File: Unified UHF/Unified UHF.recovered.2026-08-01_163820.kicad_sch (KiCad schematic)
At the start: 28 parts, among them IC6 MCP1603-330I_MC, J1 Conn_01x05, J2 Conn_01x02, J3 Conn_Coaxial, U1 AT86RF215-ZU, U3 NCS-62+, X1 TYETACSANF-26.000000

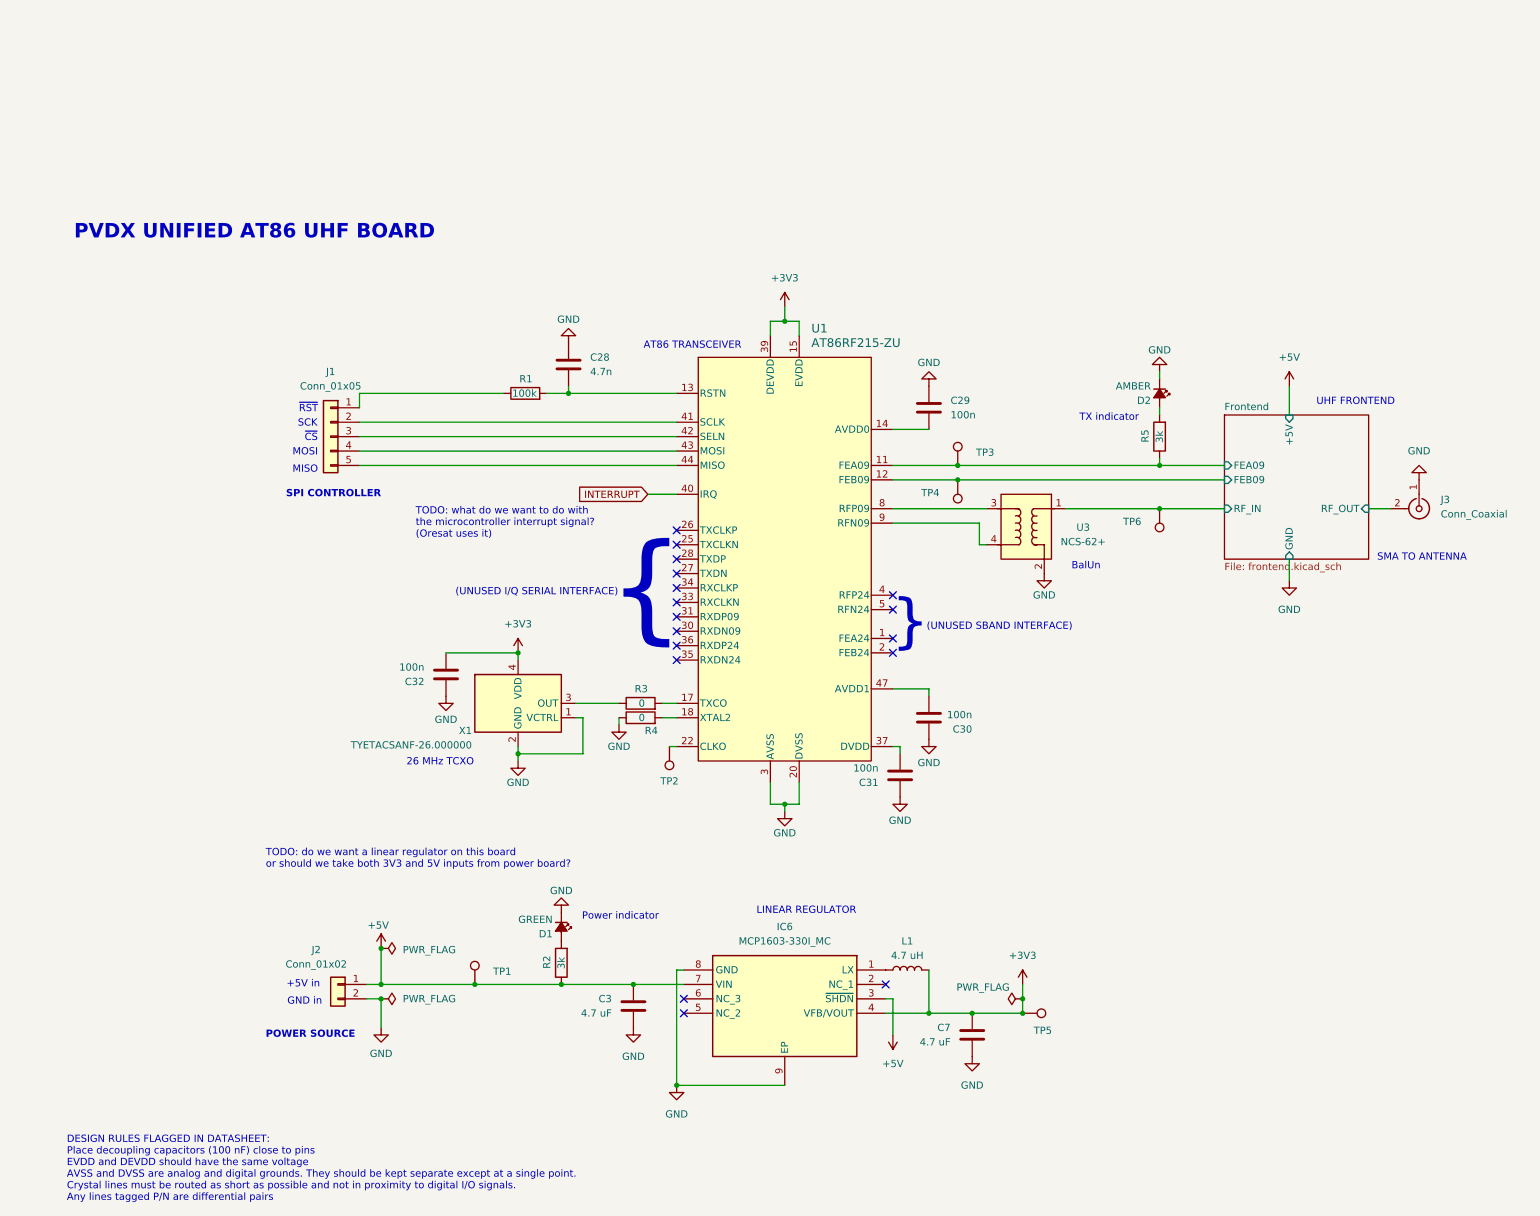
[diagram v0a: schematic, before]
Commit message: added unified radio schematic
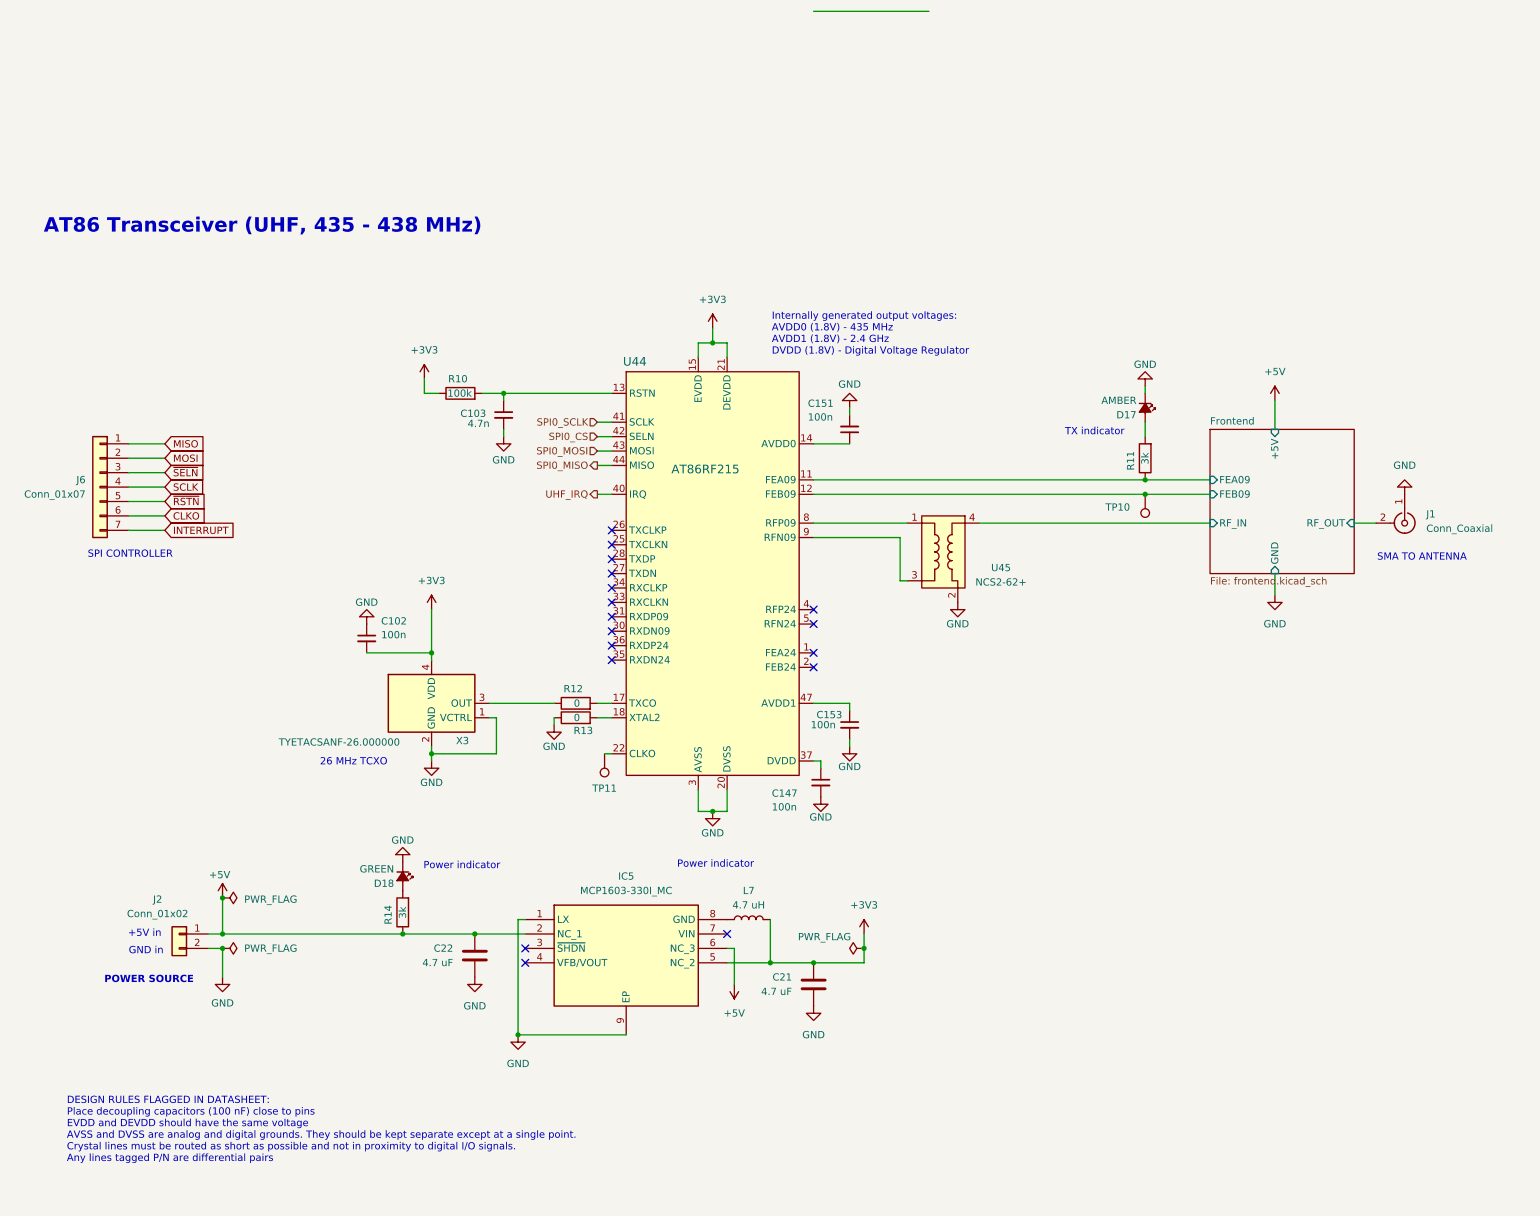
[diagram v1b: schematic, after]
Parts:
- removed C28: 4.7n, symbol Device:C
- removed C29, C30, C31, C32: 100n, symbol Device:C
- removed IC6: MCP1603-330I_MC, MCP1603:MCP1603-330, symbol MCP1603:MCP1603-330I_MC
- removed J1: Conn_01x05, symbol Connector_Generic:Conn_01x05
- removed TP1, TP3, TP5, TP6: TestPoint, TestPoint:TestPoint_THTPad_1.5x1.5mm_Drill0.7mm, symbol Connector:TestPoint
- removed U1: AT86RF215-ZU, RF Frontend Footprints:QFN-48-1EP_7x7mm_P0.5mm_EP5.6x5.6mm, symbol AT86RF215:AT86RF215-ZU
- removed U3: NCS-62+, RF Frontend Footprints:NCS262, symbol NCS2-62+:NCS2-62+_Custom
- removed X1: TYETACSANF-26.000000, RF Frontend Footprints:X_TCXO_SMD_Taitien_2.5x2.0mm, symbol TYETACSANF-26.000000:Taiten-TY-Series-TXCO
- added C102, C147, C151, C153: 100n, oresat-passives:0603-C-NOSILK, symbol Device:C_Small
- added C103: 4.7n, oresat-passives:0603-C-NOSILK, symbol Device:C_Small
- added IC5: MCP1603-330I_MC, MPC1603:MPC1603-330, symbol MCP1603:MCP1603-330I_MC
- added J6: Conn_01x07, symbol Connector_Generic:Conn_01x07
- added U44: AT86RF215, Package_DFN_QFN:QFN-48-1EP_7x7mm_P0.5mm_EP5.6x5.6mm, symbol oresat-ics:AT86RF215
- added U45: NCS2-62+, oresat-passives:2450FB15A050E_JOT, symbol oresat-passives:Balun
- added X3: TYETACSANF-26.000000, oresat-ics:X_TCXO_SMD_Taitien_2.5x2.0mm, symbol oresat-ics:Taiten-TY-Series-TXCO
- renumbered C7 to C21, C3 to C22, D2 to D17, D1 to D18, J3 to J1, L1 to L7, R1 to R10, R5 to R11, R3 to R12, R4 to R13, R2 to R14, TP4 to TP10, TP2 to TP11
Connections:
- net +3V3: now also R10.1, C102.2, IC5.5 (NC_2), U44.15 (EVDD), U44.21 (DEVDD), U44.29 (DEVDD), U44.39 (DEVDD), U44.46 (EVDD), X3.4 (VDD)
- net +5V: now also IC5.2 (NC_1), IC5.6 (NC_3)
- net Frontend/FEA09: now also U44.11 (FEA09)
- net Frontend/FEB09: now also U44.12 (FEB09)
- net Frontend/RF_IN: now also U45.4
- net GND: now also C102.1, C103.2, C147.2, C151.2, C153.2, IC5.1 (LX), IC5.9 (EP), U44.10 (AVSS), U44.16 (AVSS), U44.19 (AVSS), U44.20 (DVSS), U44.23 (DVSS), U44.24 (DVSS), U44.3 (AVSS), U44.32 (DVSS), U44.38 (DVSS), U44.45 (AVSS), U44.48 (AVSS), U44.49 (AVSS), U44.6 (AVSS), U44.7 (AVSS), U45.2 (GND), U45.6 (GND), X3.1 (VCTRL), X3.2 (GND)
- net INTERRUPT: now also J6.7 (Pin_7)
- net at TP11.1: now also U44.22 (CLKO)
- net at L7.1: now also IC5.8 (GND)
- net at R12.1: now also X3.3 (OUT)
- net at R12.2: now also U44.17 (TXCO)
- net at R13.2: now also U44.18 (XTAL2)
- net at R10.2: now also C103.1, U44.13 (RSTN)
- new net: U44.8 (RFP09), U45.1
- new net: U44.9 (RFN09), U45.3
- new net: C147.1, U44.37 (DVDD)
- new net: C151.1, U44.14 (AVDD0)
- new net: C153.1, U44.47 (AVDD1)
- new net CLKO: J6.6 (Pin_6)
- new net MISO: J6.1 (Pin_1)
- new net MOSI: J6.2 (Pin_2)
- new net SCLK: J6.4 (Pin_4)
- new net SPI0_CS: U44.42 (SELN)
- new net SPI0_MISO: U44.44 (MISO)
- new net SPI0_MOSI: U44.43 (MOSI)
- new net SPI0_SCLK: U44.41 (SCLK)
- new net UHF_IRQ: U44.40 (IRQ)
- new net ~{RSTN}: J6.5 (Pin_5)
- new net ~{SELN}: J6.3 (Pin_3)
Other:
- note added: "AT86 Transceiver (UHF, 435 - 438 MHz)"
- note added: "Internally generated output voltages: AVDD0 (1.8V) - 435 MHz AVDD1 (1.8V) - 2.4 GHz DVDD (1.8V) - Digital Voltage Regulator"
- note removed: "(UNUSED I/Q SERIAL INTERFACE)"
- note removed: "(UNUSED SBAND INTERFACE)"
- note removed: "AT86 TRANSCEIVER"
- note removed: "BalUn"
- note removed: "LINEAR REGULATOR"
- note removed: "MISO"
- note removed: "MOSI"
- note removed: "PVDX UNIFIED AT86 UHF BOARD"
- note removed: "SCK"
- note removed: "TODO: do we want a linear regulator on this board or should we take both 3V3 and 5V inputs from power board?"
- note removed: "TODO: what do we want to do with the microcontroller interrupt signal? (Oresat uses it)"
- note removed: "UHF FRONTEND"
- note removed: "{"
- note removed: "}"
- note removed: "~{CS}"
- note removed: "~{RST}"
- moved on the sheet: C21, C22, D17, D18, J1, J2, L7, R10, R11, R12, R13, R14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
